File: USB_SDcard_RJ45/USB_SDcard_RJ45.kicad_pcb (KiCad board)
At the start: 2 copper layers, 4 parts, among them J2 USB_A_Stacked, J3 USB_A_Stacked, U1 CH217K, U2 CH339F

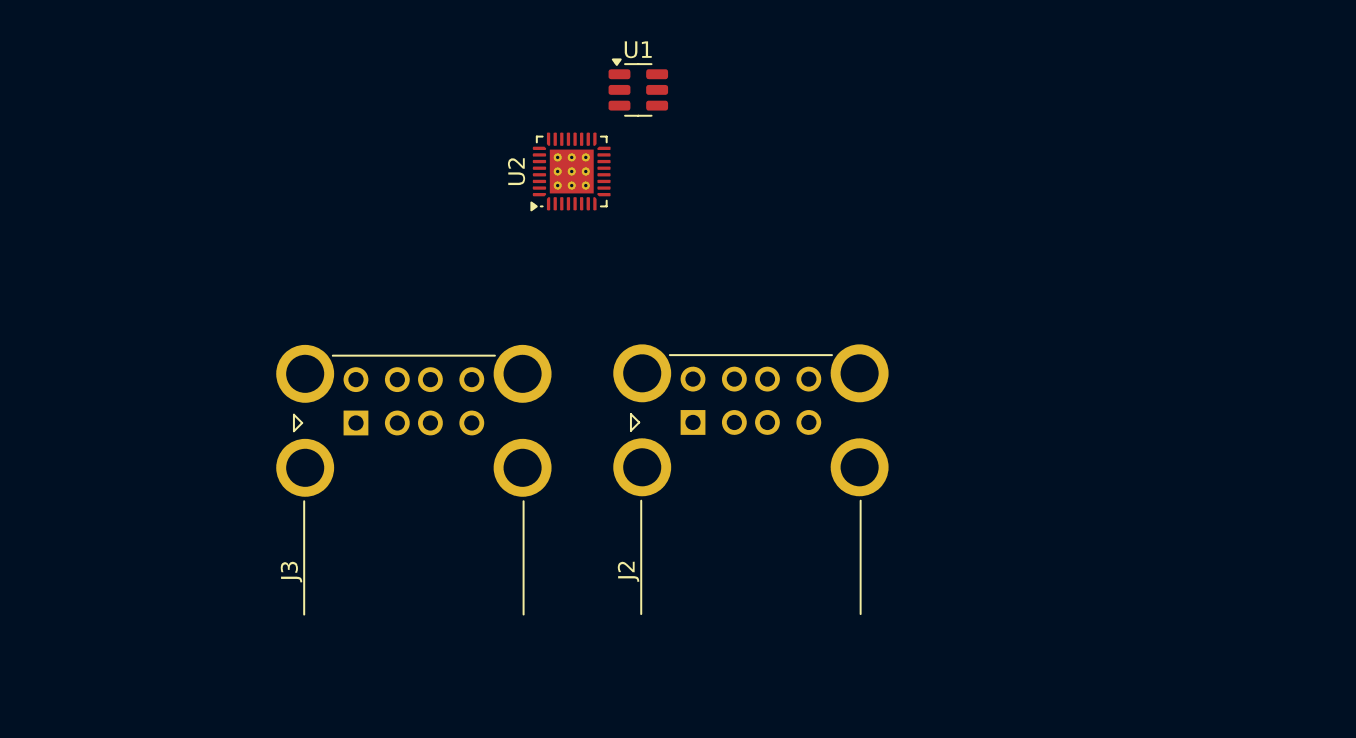
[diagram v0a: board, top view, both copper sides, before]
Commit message: Add components to schematic
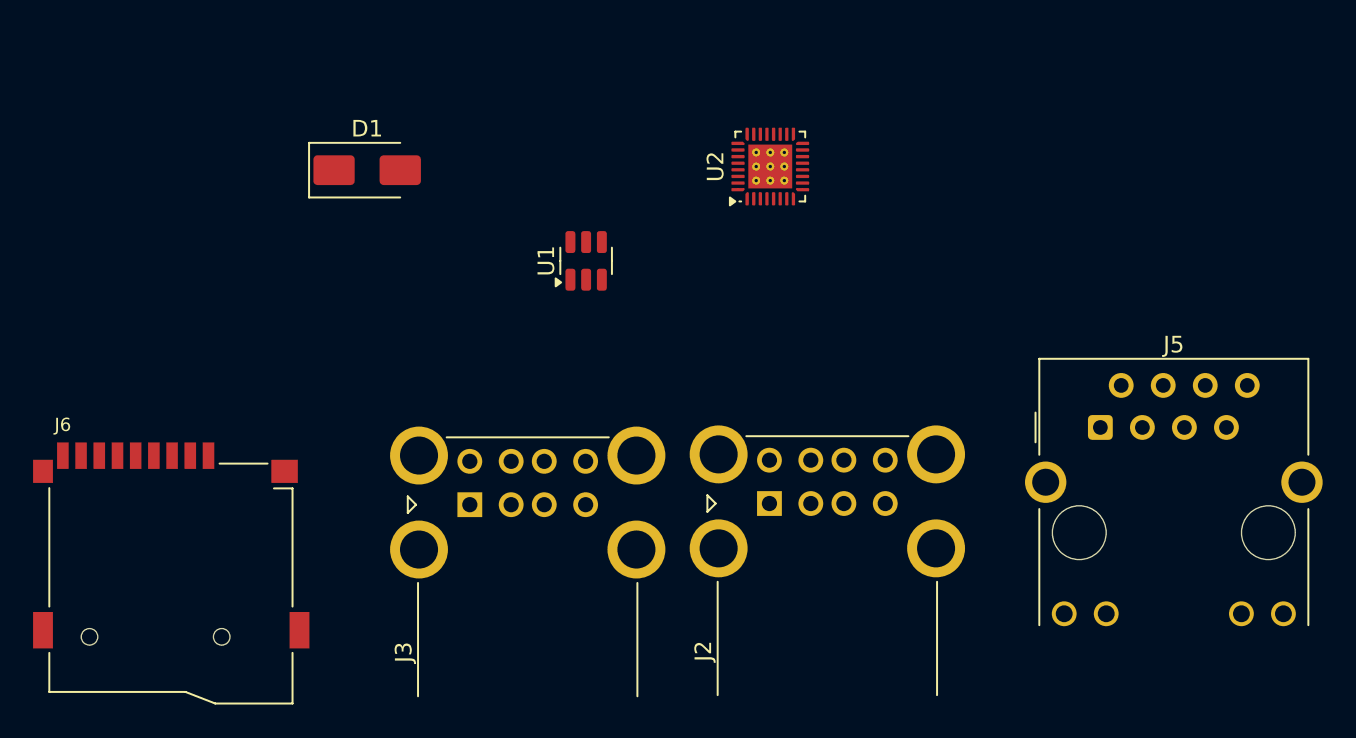
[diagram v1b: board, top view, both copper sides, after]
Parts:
- added D1: SS34, Diode_SMD:D_SMA, F.Cu at (143.1, 88.7)
- added J5: RJ45_Hanrun_HR911105A_Horizontal, Connector_RJ:RJ45_Hanrun_HR911105A_Horizontal, F.Cu at (187.4, 104.3)
- added J6: Micro_SD_Card_Det1, 3in1:MiSD-PP-9P-V2, F.Cu at (124.7, 106.0)
- moved U2 12.0 mm to (167.4, 88.5)
- moved U1 10.8 mm to (156.3, 94.2), turned to 90 degrees
- moved J3 8.47 mm to (149.3, 108.9)
- moved J2 6.73 mm to (167.4, 108.9)
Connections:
- U1 pad 2: unconnected-(U1-GND-Pad2) -> GND
- U1 pad 6: unconnected-(U1-VIN-Pad6) -> +5V
- U2 pad 1: unconnected-(U2-MDITP-Pad1) -> Net-(J5-TD+)
- U2 pad 19: unconnected-(U2-SD_D3-Pad19) -> /SD_D3
- U2 pad 2: unconnected-(U2-MDITN-Pad2) -> Net-(J5-TD-)
- U2 pad 20: unconnected-(U2-SD_D2-Pad20) -> /SD_D2
- U2 pad 21: unconnected-(U2-SD_D1-Pad21) -> /SD_D1
- U2 pad 22: unconnected-(U2-SD_D0-Pad22) -> /SD_D0
- U2 pad 23: unconnected-(U2-SD_SCK/CFG1-Pad23) -> /SD_CLK
- U2 pad 26: unconnected-(U2-LED_ACT/SDA-Pad26) -> /LED_ACT
- U2 pad 27: unconnected-(U2-LED_LINK/SCL-Pad27) -> /LED_LINK
- U2 pad 33: unconnected-(U2-GND-Pad33) -> GND
- U2 pad 4: unconnected-(U2-MDIRP-Pad4) -> Net-(J5-RD+)
- U2 pad 5: unconnected-(U2-MDIRN-Pad5) -> Net-(J5-RD-)

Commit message: Add CH339 datasheet
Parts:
- moved D1 35.8 mm to (178.9, 87.2), turned to 90 degrees
- moved J6 35.0 mm to (153.5, 86.1), turned to -90 degrees
- moved U1 5.30 mm to (159.0, 98.8)
- moved U2 1.54 mm to (168.6, 89.6), turned to 180 degrees
- moved J3 0.29 mm to (149.3, 108.6)

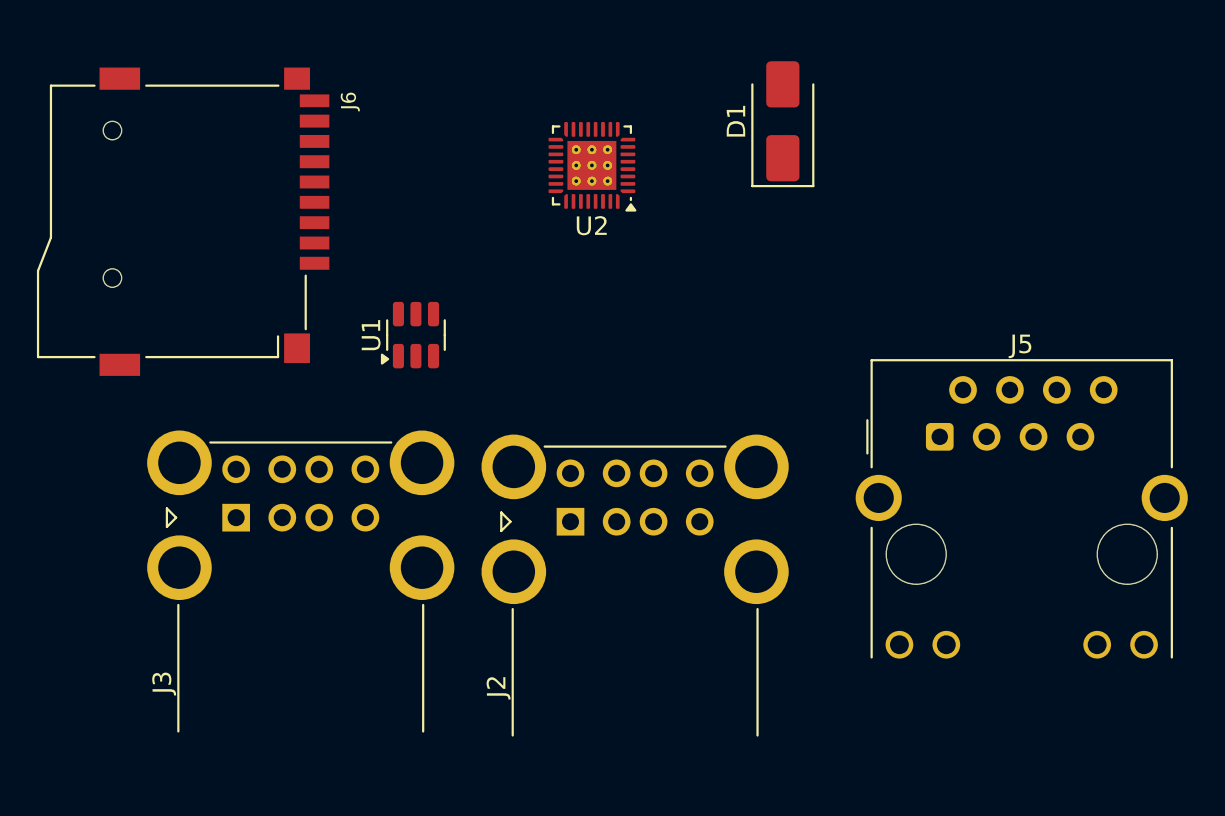
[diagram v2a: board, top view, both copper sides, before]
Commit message: Change to CH339W hub ic
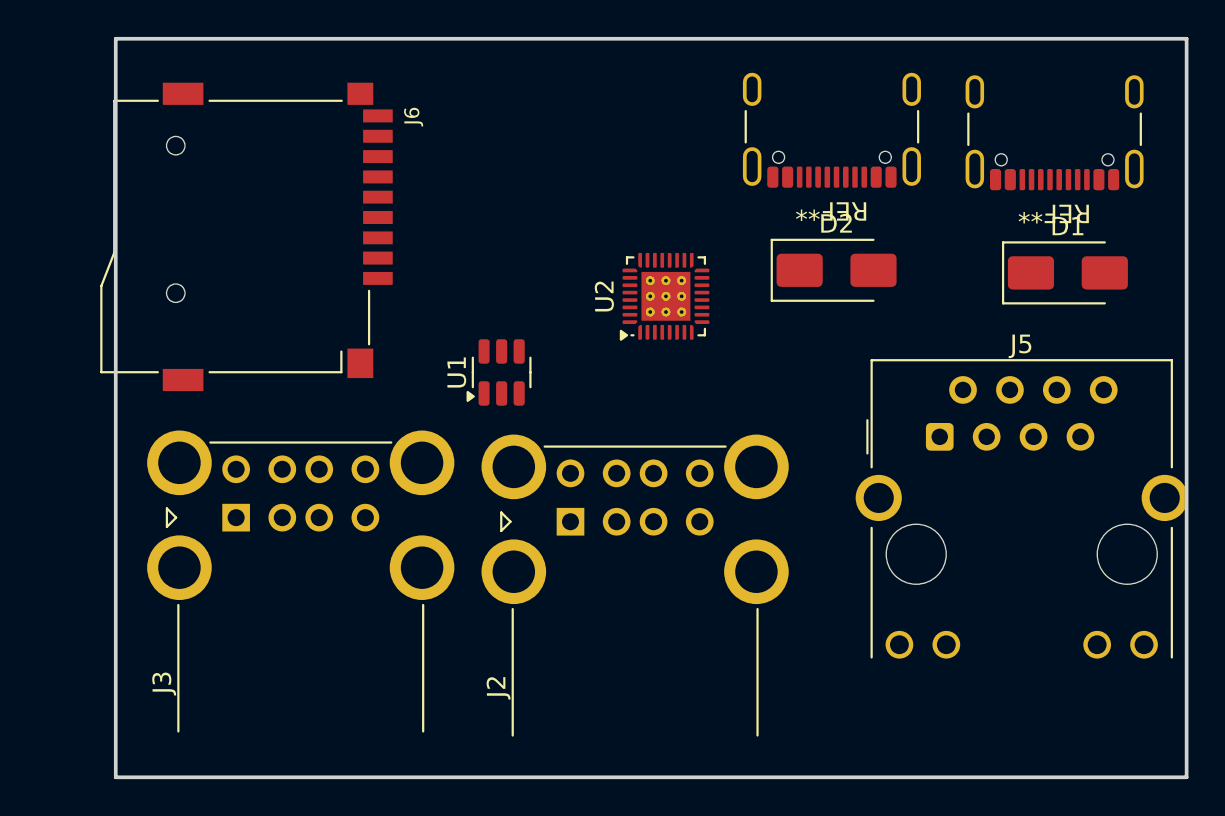
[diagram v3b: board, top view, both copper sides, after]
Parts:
- added D2: SS34, Diode_SMD:D_SMA, F.Cu at (181.8, 95.2)
- added REF**: USB_C_Receptacle_GCT_USB4105-xx-A_16P_TopMnt_Horizontal, Connector_USB:USB_C_Receptacle_GCT_USB4105-xx-A_16P_TopMnt_Horizontal, F.Cu at (181.6, 86.5)
- added REF**: USB_C_Receptacle_GCT_USB4105-xx-A_16P_TopMnt_Horizontal, Connector_USB:USB_C_Receptacle_GCT_USB4105-xx-A_16P_TopMnt_Horizontal, F.Cu at (193.6, 86.7)
- moved D1 17.5 mm to (194.3, 95.4), turned to 0 degrees
- moved U2 8.15 mm to (172.6, 96.7), turned to 90 degrees
- moved U1 5.06 mm to (163.7, 100.8)
- moved J6 3.53 mm to (157.0, 86.9)
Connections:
- J5 pad 10: unconnected-(J5-Pad10) -> /LED_ACT
- J5 pad 11: unconnected-(J5-Pad11) -> /LED_LINK
- J5 pad 12: unconnected-(J5-Pad12) -> Net-(J5-Pad12)
- J5 pad 8: unconnected-(J5-Pad8) -> GND
- J5 pad 9: unconnected-(J5-Pad9) -> Net-(J5-Pad9)
- J6 pad 5: unconnected-(J6-CLK-Pad5) -> /SD_CLK
- U1 pad 3: unconnected-(U1-~{FLAG}-Pad3) -> /OVCUR#
- U2 pad 17: unconnected-(U2-OVCUR#-Pad17) -> /OVCUR#
- U2 pad 18: unconnected-(U2-PWREN#-Pad18) -> /EN
- U2 pad 6: unconnected-(U2-DMU-Pad6) -> /HOST_DN
- U2 pad 7: unconnected-(U2-DPU-Pad7) -> /HOST_DP
- U2 pad 8: unconnected-(U2-XO-Pad8) -> Net-(U2-XO)
- U2 pad 9: unconnected-(U2-XI-Pad9) -> Net-(U2-XI)
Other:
- board outline added: 58 x 40 mm

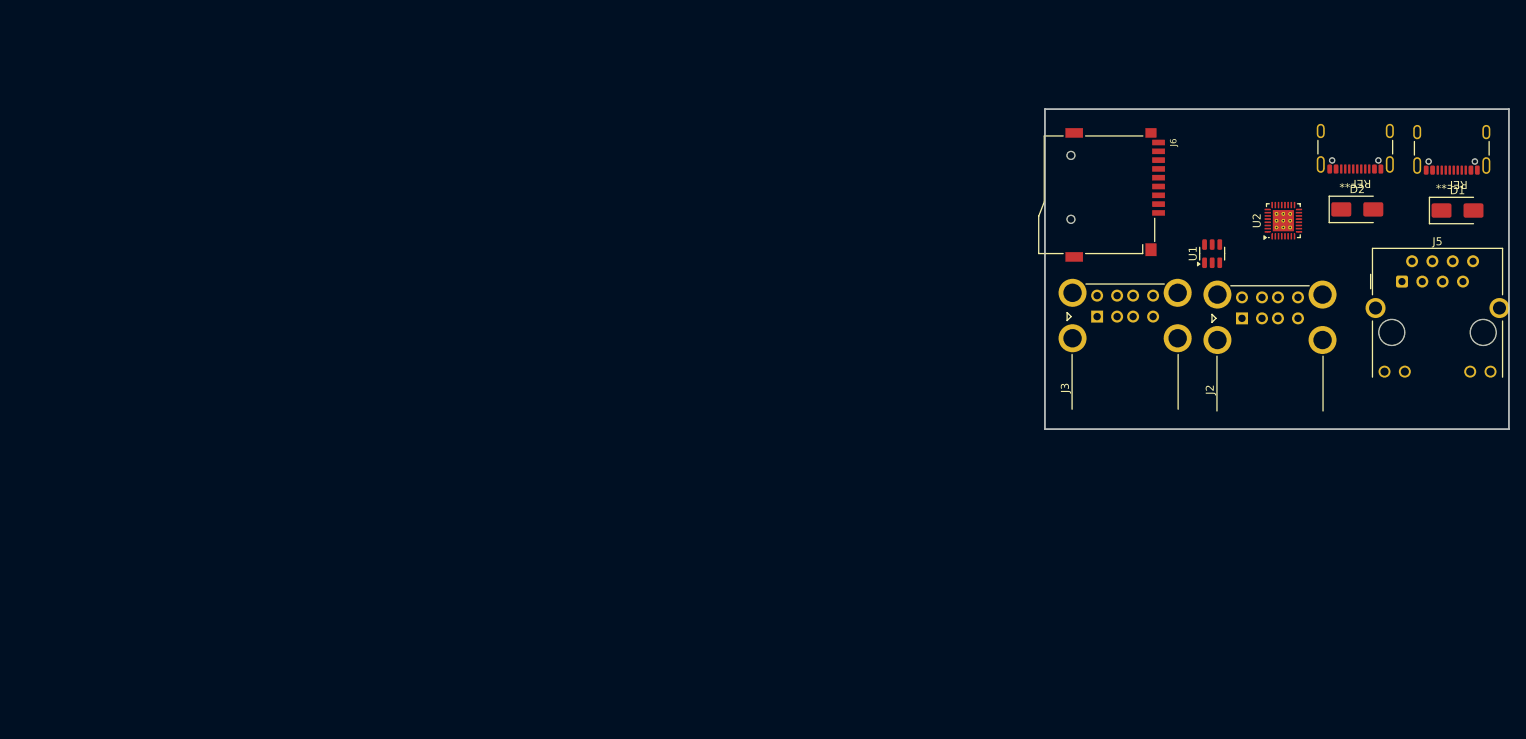
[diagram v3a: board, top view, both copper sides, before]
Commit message: Change layout to match CH339W
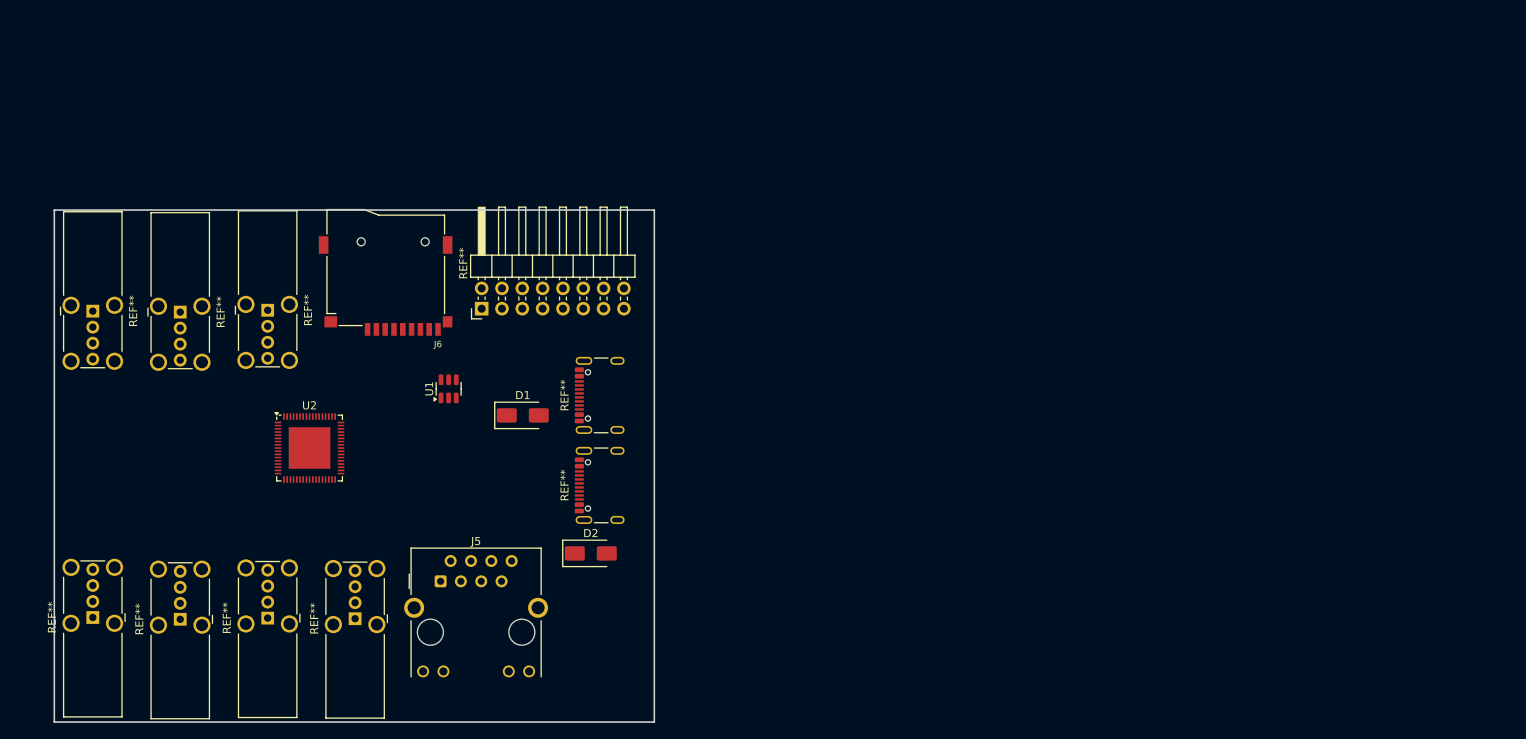
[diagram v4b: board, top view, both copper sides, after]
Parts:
- removed J2, J3: USB_A_Stacked, Connector_USB:USB_A_CUI_UJ2-ADH-TH_Horizontal_Stacked
- added REF**: PinHeader_2x08_P2.54mm_Horizontal, Connector_PinHeader_2.54mm:PinHeader_2x08_P2.54mm_Horizontal, F.Cu at (72.4, 107.7)
- added REF**: USB_A_Wuerth_614004134726_Horizontal, Connector_USB:USB_A_Wuerth_614004134726_Horizontal, F.Cu at (45.6, 107.9)
- added REF**: USB_A_Wuerth_614004134726_Horizontal, Connector_USB:USB_A_Wuerth_614004134726_Horizontal, F.Cu at (34.7, 108.1)
- added REF**: USB_A_Wuerth_614004134726_Horizontal, Connector_USB:USB_A_Wuerth_614004134726_Horizontal, F.Cu at (45.6, 146.3)
- added REF**: USB_A_Wuerth_614004134726_Horizontal, Connector_USB:USB_A_Wuerth_614004134726_Horizontal, F.Cu at (56.5, 146.4)
- added REF**: USB_A_Wuerth_614004134726_Horizontal, Connector_USB:USB_A_Wuerth_614004134726_Horizontal, F.Cu at (23.8, 108.0)
- added REF**: USB_A_Wuerth_614004134726_Horizontal, Connector_USB:USB_A_Wuerth_614004134726_Horizontal, F.Cu at (23.8, 146.3)
- added REF**: USB_A_Wuerth_614004134726_Horizontal, Connector_USB:USB_A_Wuerth_614004134726_Horizontal, F.Cu at (34.7, 146.5)
- U2: value CH339F -> CH339W; footprint Package_DFN_QFN:QFN-32-1EP_4x4mm_P0.4mm_EP2.65x2.65mm_ThermalVias -> Package_DFN_QFN:QFN-68-1EP_8x8mm_P0.4mm_EP5.2x5.2mm
- moved J5 125.9 mm to (67.2, 141.7)
- moved U2 125.0 mm to (50.8, 125.1), turned to 0 degrees
- moved D1 119.6 mm to (77.5, 121.0)
- moved REF** 113.8 mm to (88.2, 129.8), turned to 90 degrees
- moved D2 105.0 mm to (86.0, 138.2)
- moved REF** 98.6 mm to (88.2, 118.5), turned to 90 degrees
- moved U1 96.9 mm to (68.2, 117.7)
- moved J6 93.0 mm to (66.9, 110.2), turned to 180 degrees
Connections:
- J5 pad 1: Net-(J5-TD+) -> unconnected-(J5-TD+-Pad1)
- J5 pad 2: Net-(J5-TD-) -> unconnected-(J5-TD--Pad2)
- J5 pad 3: Net-(J5-RD+) -> unconnected-(J5-RD+-Pad3)
- J5 pad 6: Net-(J5-RD-) -> unconnected-(J5-RD--Pad6)
- U2 pad 1: Net-(J5-TD+) -> unconnected-(U2-MDITP-Pad1)
- U2 pad 11: Net-(J2-D1-) -> unconnected-(U2-VDD33-Pad11)
- U2 pad 12: Net-(J2-D1+) -> unconnected-(U2-DMU-Pad12)
- U2 pad 13: Net-(J2-D2-) -> unconnected-(U2-DPU-Pad13)
- U2 pad 14: Net-(J2-D2+) -> unconnected-(U2-GND-Pad14)
- U2 pad 17: /OVCUR# -> unconnected-(U2-AVDDK-Pad17)
- U2 pad 18: /EN -> unconnected-(U2-DM1-Pad18)
- U2 pad 19: /SD_D3 -> unconnected-(U2-DP1-Pad19)
- U2 pad 2: Net-(J5-TD-) -> unconnected-(U2-MDITN-Pad2)
- U2 pad 20: /SD_D2 -> unconnected-(U2-DM2-Pad20)
- U2 pad 21: /SD_D1 -> unconnected-(U2-DP2-Pad21)
- U2 pad 22: /SD_D0 -> unconnected-(U2-GND-Pad22)
- U2 pad 23: /SD_CLK -> unconnected-(U2-VDD33-Pad23)
- U2 pad 26: /LED_ACT -> unconnected-(U2-DM4-Pad26)
- U2 pad 27: /LED_LINK -> unconnected-(U2-DP4-Pad27)
- U2 pad 29: Net-(J3-D2-) -> unconnected-(U2-DP5-Pad29)
- U2 pad 30: Net-(J3-D2+) -> unconnected-(U2-VDD33-Pad30)
- U2 pad 31: Net-(J3-D1-) -> unconnected-(U2-LED_ACT/CFG0-Pad31)
- U2 pad 32: Net-(J3-D1+) -> unconnected-(U2-RXD/OVCUR3#-Pad32)
- U2 pad 33: GND -> unconnected-(U2-TXD/OVCUR2#-Pad33)
- U2 pad 4: Net-(J5-RD+) -> unconnected-(U2-MDIRP-Pad4)
- U2 pad 5: Net-(J5-RD-) -> unconnected-(U2-MDIRN-Pad5)
- U2 pad 6: /HOST_DN -> unconnected-(U2-GND-Pad6)
- U2 pad 7: /HOST_DP -> unconnected-(U2-DM6-Pad7)
- U2 pad 8: Net-(U2-XO) -> unconnected-(U2-DP6-Pad8)
- U2 pad 9: Net-(U2-XI) -> unconnected-(U2-DM7-Pad9)
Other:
- board size 58 x 40 mm -> 75 x 64 mm

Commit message: Change USB type
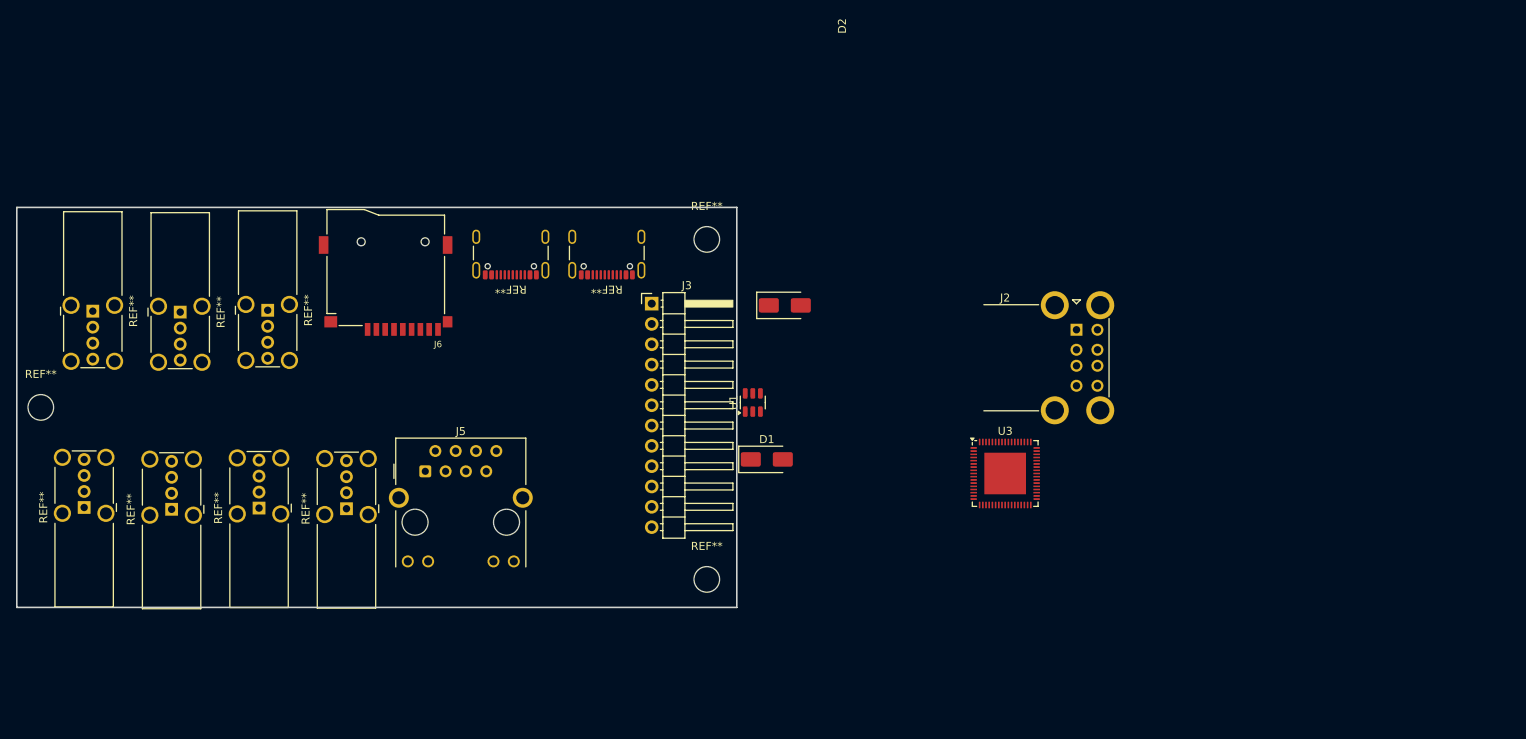
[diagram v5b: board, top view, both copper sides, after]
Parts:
- removed the REF** at (72.4, 107.7)
- removed U2: CH339W, Package_DFN_QFN:QFN-68-1EP_8x8mm_P0.4mm_EP5.2x5.2mm
- added J2: USB_A_Stacked, Connector_USB:USB_A_CUI_UJ2-ADH-TH_Horizontal_Stacked, F.Cu at (146.7, 110.3)
- added J3: Conn_01x12_Pin, Connector_PinHeader_2.54mm:PinHeader_1x12_P2.54mm_Horizontal, F.Cu at (93.6, 107.0)
- added REF**: MountingHole_3.2mm_M3, MountingHole:MountingHole_3.2mm_M3, F.Cu at (17.2, 120.0)
- added REF**: MountingHole_3.2mm_M3, MountingHole:MountingHole_3.2mm_M3, F.Cu at (100.5, 99.0)
- added REF**: MountingHole_3.2mm_M3, MountingHole:MountingHole_3.2mm_M3, F.Cu at (100.5, 141.5)
- added U3: CH339W, Package_DFN_QFN:QFN-68-1EP_8x8mm_P0.4mm_EP5.2x5.2mm, F.Cu at (137.8, 128.3)
- moved D2 39.4 mm to (110.2, 107.2)
- moved U1 38.1 mm to (106.2, 119.4)
- moved D1 31.0 mm to (108.0, 126.5)
- moved REF** 30.0 mm to (88.0, 99.8), turned to 180 degrees
- moved REF** 22.4 mm to (76.0, 99.8), turned to 180 degrees
- moved J5 13.9 mm to (65.3, 128.0)
- moved REF** 13.8 mm to (33.6, 132.7)
- moved REF** 13.8 mm to (44.5, 132.6)
- moved REF** 13.8 mm to (55.5, 132.7)
- moved REF** 13.8 mm to (22.7, 132.5)
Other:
- board size 75 x 64 mm -> 90 x 50 mm
